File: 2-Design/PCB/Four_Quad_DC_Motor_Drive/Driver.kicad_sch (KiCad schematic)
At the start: 15 parts, among them Q1 SPW47N60, Q2 SPW47N60, Q3 SPW47N60, Q4 SPW47N60, U1 HCPL-3120, U2 HCPL-3120, U3 HCPL-3120, U4 HCPL-3120

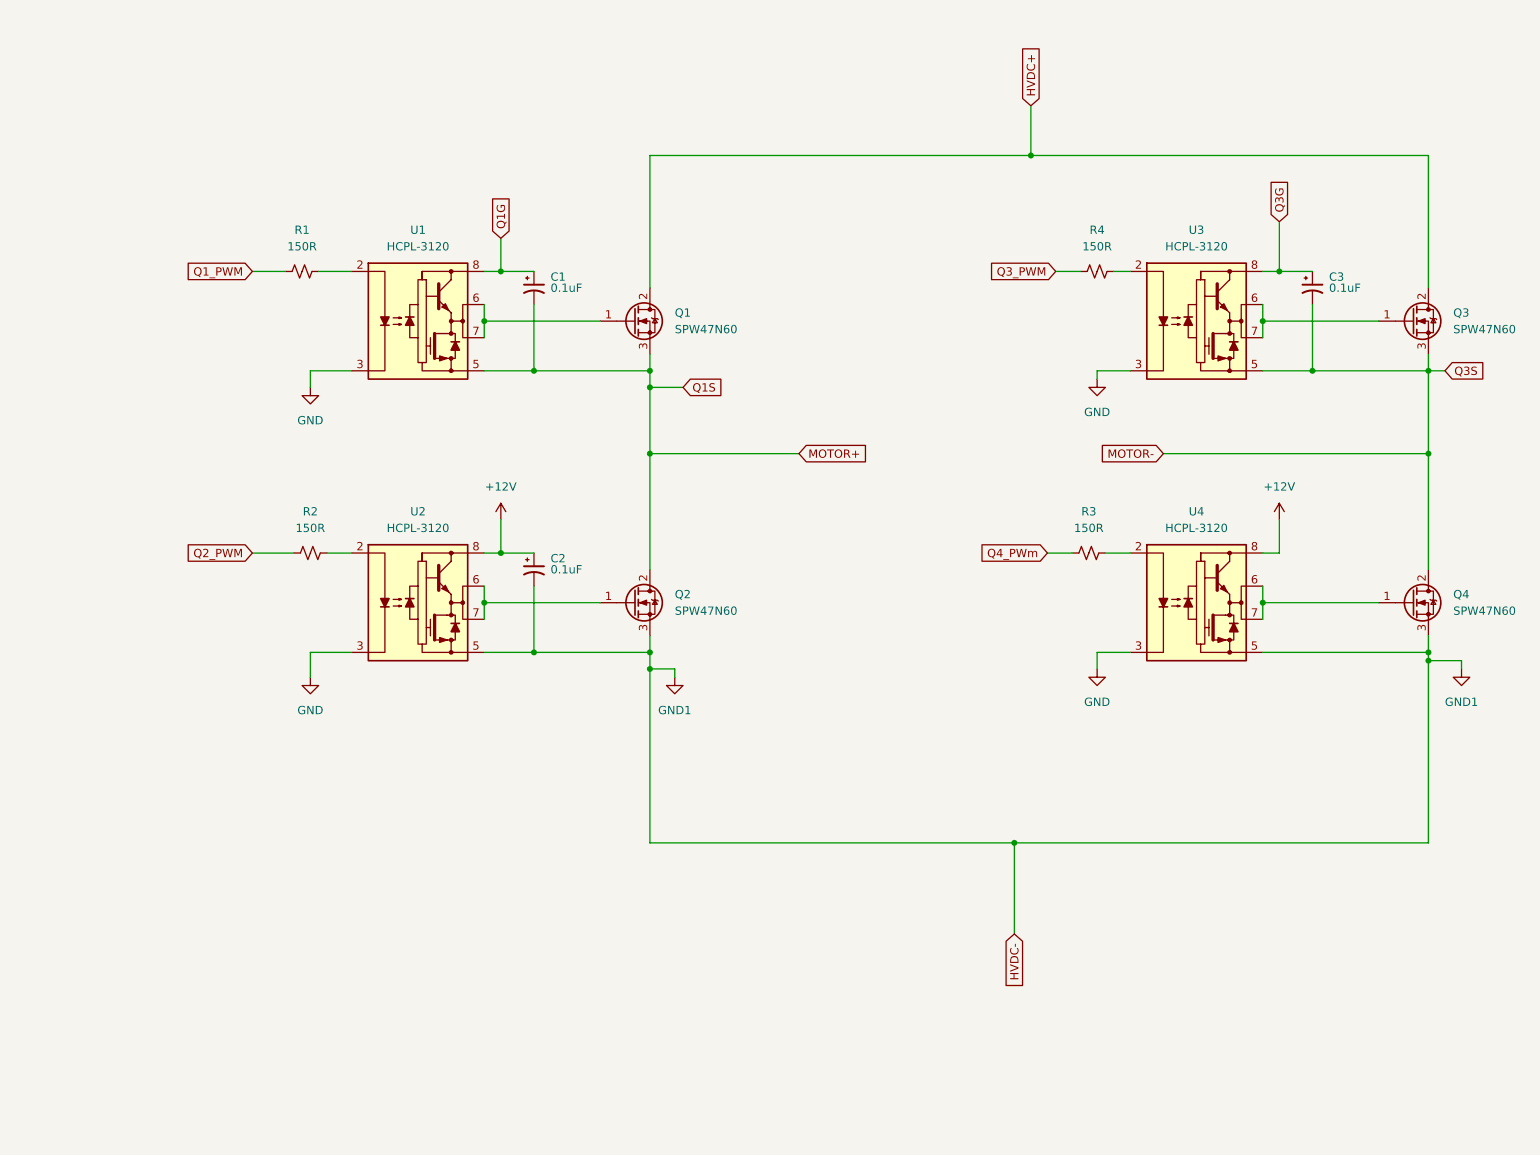
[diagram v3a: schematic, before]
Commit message: Gate driver changed, plus other rearrangements on the schematics
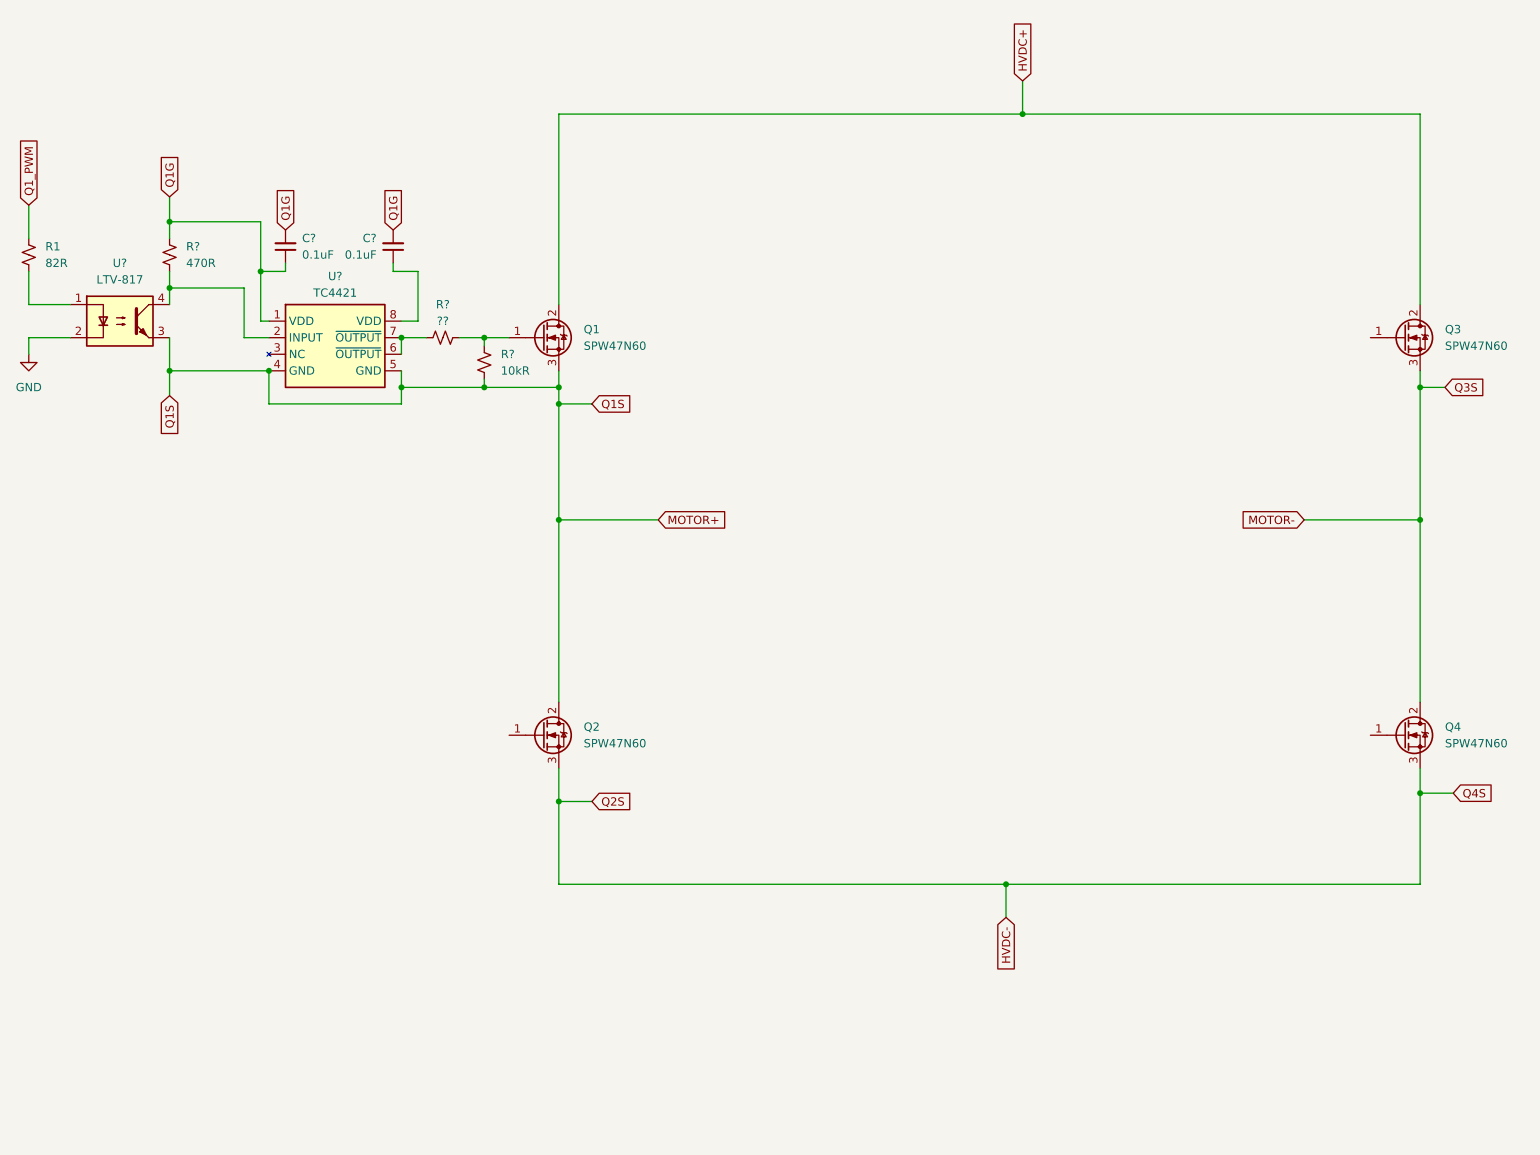
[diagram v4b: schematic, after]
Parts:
- removed C1, C2, C3: 0.1uF, symbol Device:C_Polarized_Small_US
- removed R2, R3, R4: 150R, symbol Device:R_Small_US
- removed U1, U2, U3, U4: HCPL-3120, Package_DIP:DIP-8_W7.62mm, symbol Driver_FET:HCPL-3120
- added C? (x2): 0.1uF, Capacitor_SMD:C_1206_3216Metric_Pad1.33x1.80mm_HandSolder, symbol Device:C_Small
- added R?: 470R, symbol Device:R_Small_US
- added R?: 10kR, symbol Device:R_Small_US
- added R?: ??, symbol Device:R_Small_US
- added U?: LTV-817, Package_DIP:DIP-4_W7.62mm, symbol Isolator:LTV-817
- added U?: TC4421, Package_SO:SOIC-8_3.9x4.9mm_P1.27mm, symbol Driver_FET:TC4421
- R1: value 150R -> 82R
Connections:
- net GND: now also U?.2
- net MOTOR+: now also R?.1, U?.3, U?.4 (GND), U?.5 (GND)
- net Q1G: now also C?.1, C?.2, C?.2, R?.2, U?.1 (VDD)
- net Q1_PWM: now also R1.2; no longer R1.1
- net at Q1.1 (G): now also R?.1, R?.2
- net GND1 renamed HVDC-
- new net: C?.1, U?.8 (VDD)
- new net: R1.1, U?.1
- new net: R?.1, U?.2 (INPUT), U?.4
- new net: R?.2, U?.6 (~{OUTPUT}), U?.7 (~{OUTPUT})
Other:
- moved on the sheet: Q1, Q2, Q3, Q4, R1

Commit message: Gate drivers finished, controller pins to be arranged
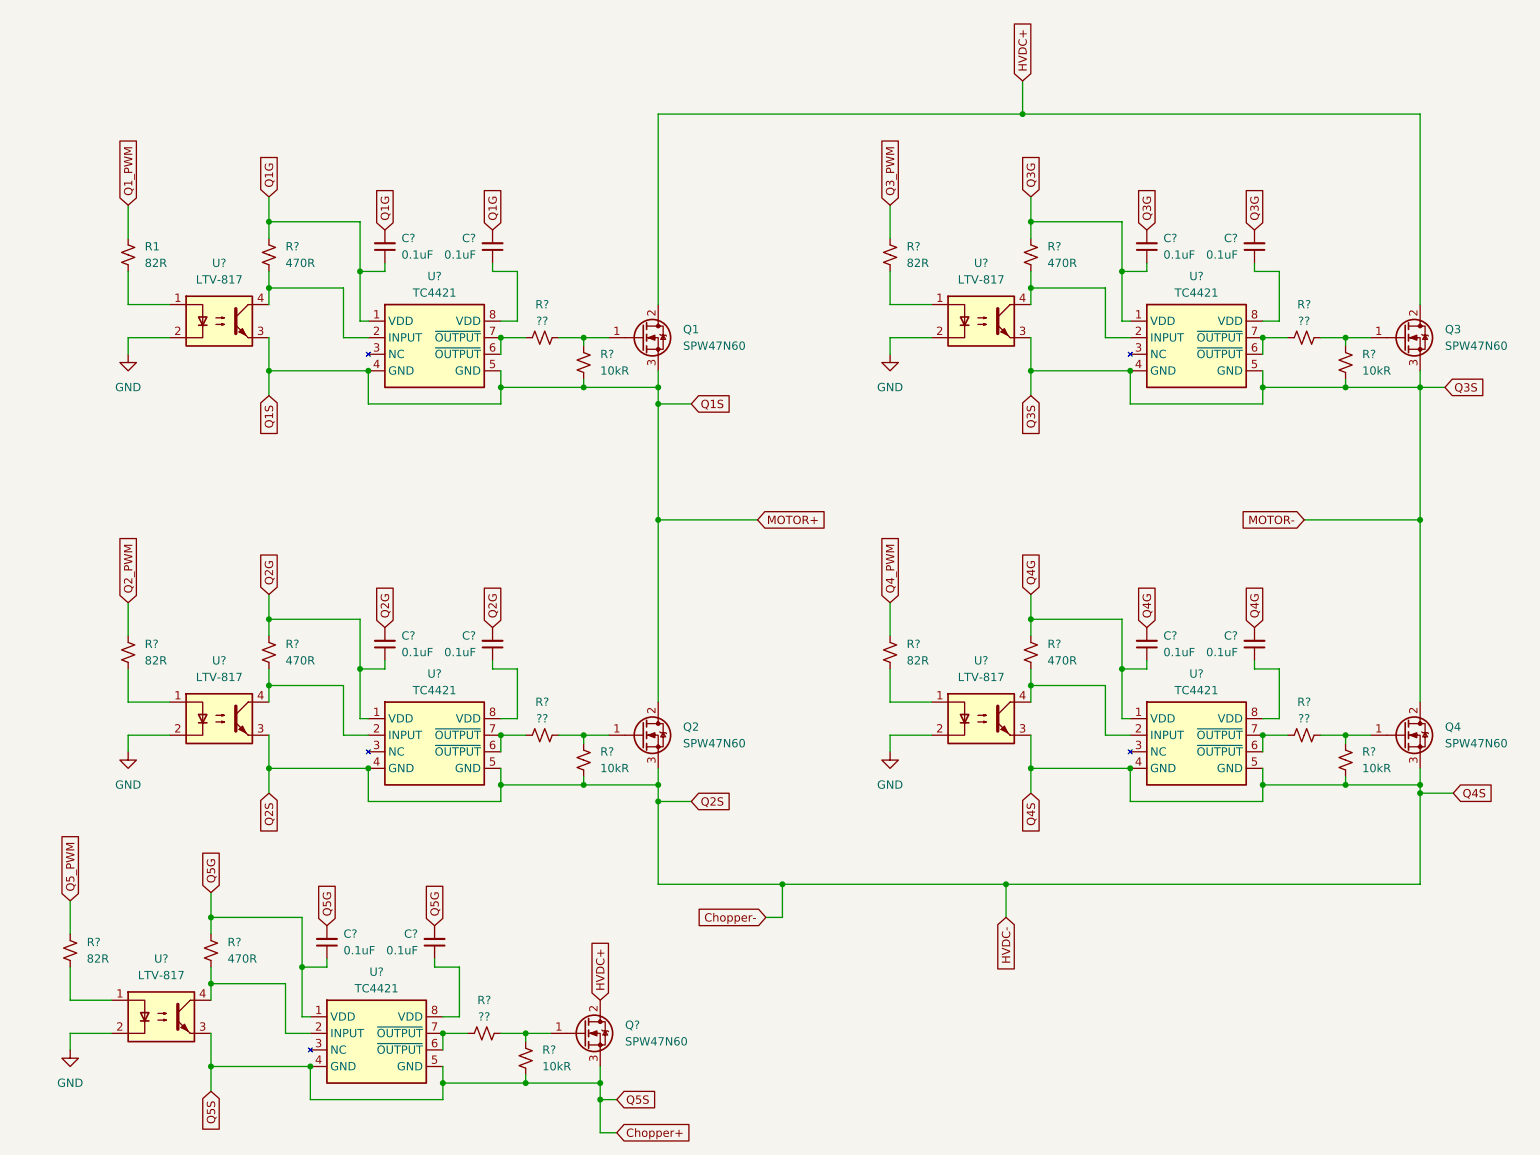
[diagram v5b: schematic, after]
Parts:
- added C? (x8): 0.1uF, Capacitor_SMD:C_1206_3216Metric_Pad1.33x1.80mm_HandSolder, symbol Device:C_Small
- added Q?: SPW47N60, symbol Device:Q_NMOS_GDS
- added R? (x4): 82R, symbol Device:R_Small_US
- added R? (x4): 10kR, symbol Device:R_Small_US
- added R? (x4): 470R, symbol Device:R_Small_US
- added R? (x4): ??, symbol Device:R_Small_US
- added U? (x4): TC4421, Package_SO:SOIC-8_3.9x4.9mm_P1.27mm, symbol Driver_FET:TC4421
- added U? (x4): LTV-817, Package_DIP:DIP-4_W7.62mm, symbol Isolator:LTV-817
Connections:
- net GND: now also U?.2, U?.2, U?.2, U?.2
- net HVDC+: now also Q?.2 (D)
- net MOTOR-: now also R?.1, U?.3, U?.4 (GND), U?.5 (GND)
- net at Q3.1 (G): now also R?.1, R?.2
- net at Q2.1 (G): now also R?.1, R?.2
- net at Q4.1 (G): now also R?.1, R?.2
- net HVDC- renamed Chopper-
- net Chopper-: now also R?.1, R?.1, U?.3, U?.3, U?.4 (GND), U?.4 (GND), U?.5 (GND), U?.5 (GND)
- new net: R?.1, U?.2 (INPUT), U?.4 (x4)
- new net: R?.2, U?.6 (~{OUTPUT}), U?.7 (~{OUTPUT}) (x4)
- new net: C?.1, U?.8 (VDD) (x4)
- new net: R?.1, U?.1 (x4)
- new net: Q?.1 (G), R?.1, R?.2
- new net Chopper+: Q?.3 (S), R?.1, U?.3, U?.4 (GND), U?.5 (GND)
- new net Q2G: C?.1, C?.2, C?.2, R?.2, U?.1 (VDD)
- new net Q2_PWM: R?.2
- new net Q3G: C?.1, C?.2, C?.2, R?.2, U?.1 (VDD)
- new net Q3_PWM: R?.2
- new net Q4G: C?.1, C?.2, C?.2, R?.2, U?.1 (VDD)
- new net Q4_PWM: R?.2
- new net Q5G: C?.1, C?.2, C?.2, R?.2, U?.1 (VDD)
- new net Q5_PWM: R?.2
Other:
- moved on the sheet: C?, Q1, Q2, R1, R?, U?
